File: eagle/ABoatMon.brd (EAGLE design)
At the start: 78.7 x 61 mm, 30 parts, among them J1 5V, J2 GND, J3 GND, J4 5V, X1 MKDSN1,5/2-5,08

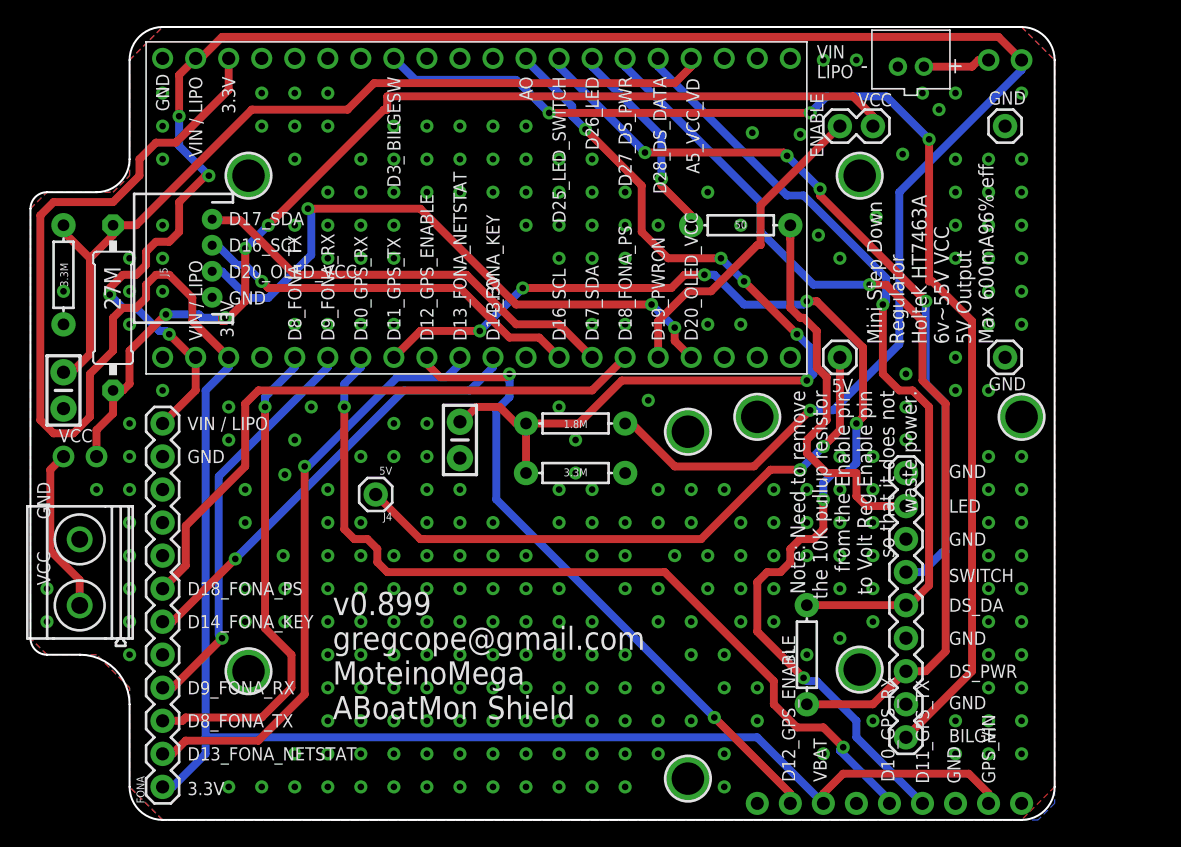
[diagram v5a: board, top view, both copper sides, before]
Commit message: fixed vcc
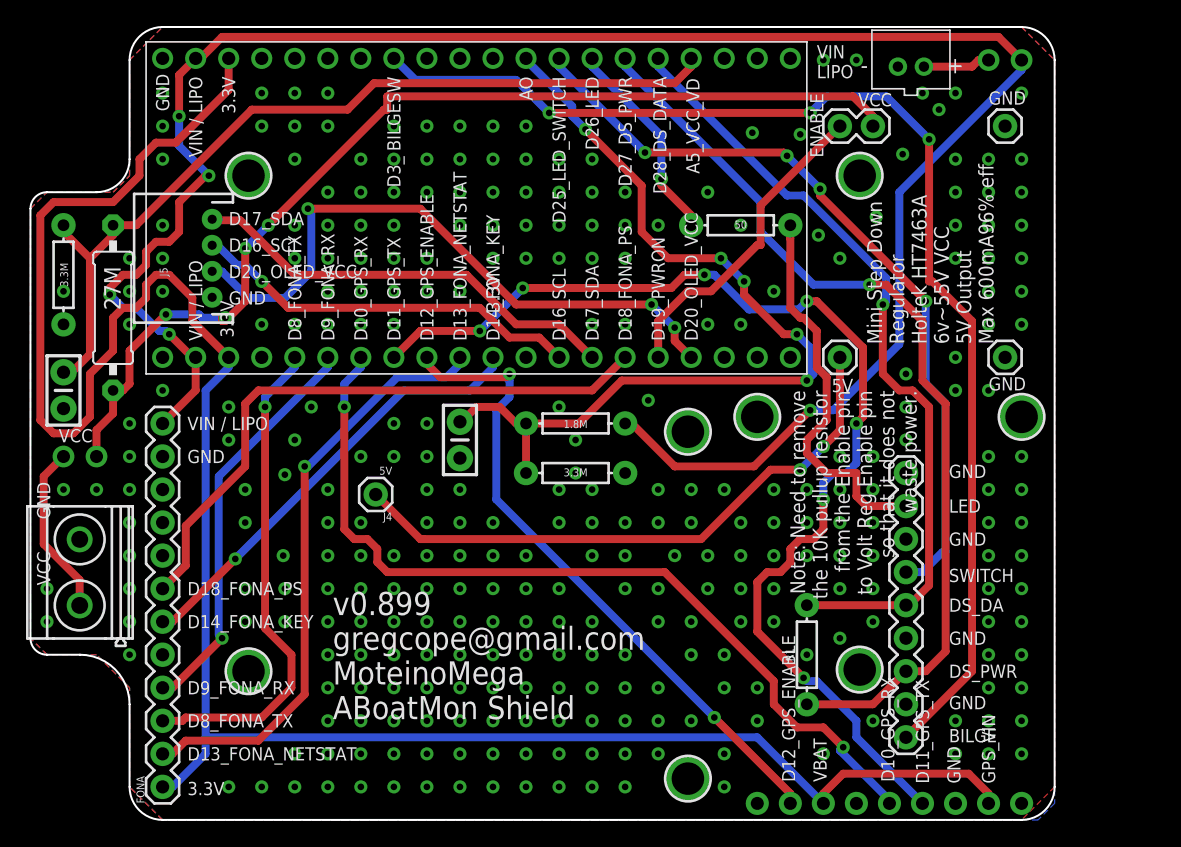
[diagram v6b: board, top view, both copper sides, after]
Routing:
- net D20_OLED_VCC: track 48.4 -> 49.2 mm
- net A0: track 69.4 -> 70.0 mm
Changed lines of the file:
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@@
 <?xml version="1.0" encoding="utf-8"?>
 <!DOCTYPE eagle SYSTEM "eagle.dtd">
-<eagle version="9.1.0">
+<eagle version="9.3.0">
 <drawing>
 <settings>
@@
 <via x="74.93" y="5.08" extent="1-16" drill="0.508"/>
 <via x="8.89" y="12.7" extent="1-16" drill="0.508"/>
-<via x="6.35" y="25.4" extent="1-16" drill="0.508"/>
+<via x="3.81" y="25.4" extent="1-16" drill="0.508"/>
 <via x="2.54" y="17.78" extent="1-16" drill="0.508"/>
 <via x="72.39" y="55.88" extent="1-16" drill="0.508"/>
@@
 <via x="24.13" y="38.1" extent="1-16" drill="0.508"/>
 <via x="26.67" y="38.1" extent="1-16" drill="0.508"/>
-<via x="29.21" y="38.1" extent="1-16" drill="0.508"/>
+<via x="26.67" y="40.64" extent="1-16" drill="0.508"/>
 <via x="24.13" y="43.18" extent="1-16" drill="0.508"/>
 <via x="26.67" y="43.18" extent="1-16" drill="0.508"/>
@@
 <via x="50.8" y="20.32" extent="1-16" drill="0.508"/>
 <via x="58.42" y="25.4" extent="1-16" drill="0.508"/>
+<via x="6.35" y="25.4" extent="1-16" drill="0.508"/>
+<via x="19.05" y="38.1" extent="1-16" drill="0.508"/>
+<via x="31.75" y="43.18" extent="1-16" drill="0.508"/>
+<via x="36.83" y="43.18" extent="1-16" drill="0.508"/>
+<via x="39.37" y="43.18" extent="1-16" drill="0.508"/>
+<via x="36.83" y="45.72" extent="1-16" drill="0.508"/>
+<via x="34.29" y="45.72" extent="1-16" drill="0.508"/>
+<via x="21.59" y="43.18" extent="1-16" drill="0.508"/>
+<via x="24.13" y="40.64" extent="1-16" drill="0.508"/>
+<via x="29.21" y="38.1" extent="1-16" drill="0.508"/>
+<via x="29.21" y="40.64" extent="1-16" drill="0.508"/>
+<via x="31.75" y="40.64" extent="1-16" drill="0.508"/>
+<via x="34.29" y="40.64" extent="1-16" drill="0.508"/>
+<via x="58.42" y="40.64" extent="1-16" drill="0.508"/>
 </signal>
 <signal name="VIN" class="1">
@@
 <wire x1="54.356" y1="43.18" x2="50.292" y2="43.18" width="0.6096" layer="1"/>
 <wire x1="56.134" y1="41.402" x2="54.356" y2="43.18" width="0.6096" layer="16"/>
-<wire x1="60.198" y1="37.338" x2="56.134" y2="41.402" width="0.6096" layer="1"/>
+<wire x1="60.198" y1="37.338" x2="59.182" y2="37.338" width="0.6096" layer="1"/>
+<wire x1="59.182" y1="37.338" x2="56.134" y2="40.386" width="0.6096" layer="1"/>
+<wire x1="56.134" y1="40.386" x2="56.134" y2="41.402" width="0.6096" layer="1"/>
 <wire x1="61.214" y1="36.322" x2="60.198" y2="37.338" width="0.6096" layer="16"/>
 <wire x1="61.214" y1="34.544" x2="61.214" y2="36.322" width="0.6096" layer="16"/>
@@
 <wire x1="46.736" y1="33.782" x2="60.96" y2="33.782" width="0.6096" layer="1"/>
 <wire x1="43.434" y1="30.48" x2="46.736" y2="33.782" width="0.6096" layer="1"/>
-<wire x1="39.624" y1="30.48" x2="43.434" y2="30.48" width="0.6096" layer="1"/>
+<wire x1="39.37" y1="30.48" x2="43.434" y2="30.48" width="0.6096" layer="1"/>
 <wire x1="39.37" y1="58.42" x2="39.37" y2="58.547" width="0.6096" layer="16"/>
-<wire x1="39.624" y1="30.48" x2="39.37" y2="30.48" width="0.6096" layer="1"/>
-<wire x1="39.37" y1="30.226" x2="39.37" y2="26.67" width="0.6096" layer="1"/>
-<wire x1="39.37" y1="30.226" x2="39.37" y2="30.48" width="0.6096" layer="1"/>
+<wire x1="39.37" y1="30.48" x2="39.37" y2="26.67" width="0.6096" layer="1"/>
 <via x="43.942" y="53.086" extent="1-16" drill="0.508"/>
 <via x="54.356" y="43.18" extent="1-16" drill="0.508"/>
@@
 <contactref element="VCC" pad="2"/>
 <contactref element="X1" pad="1"/>
-<wire x1="2.794" y1="26.924" x2="3.81" y2="27.94" width="0.6096" layer="1"/>
-<wire x1="2.794" y1="20.701" x2="2.794" y2="26.924" width="0.6096" layer="1"/>
+<wire x1="2.286" y1="26.416" x2="3.81" y2="27.94" width="0.6096" layer="1"/>
+<wire x1="2.286" y1="21.209" x2="2.286" y2="26.416" width="0.6096" layer="1"/>
 <wire x1="5.055" y1="16.4889" x2="5.055" y2="18.44" width="0.6096" layer="1"/>
-<wire x1="5.055" y1="18.44" x2="2.794" y2="20.701" width="0.6096" layer="1"/>
+<wire x1="5.055" y1="18.44" x2="2.286" y2="21.209" width="0.6096" layer="1"/>
 </signal>
 <signal name="5V" class="1">
@@
 <contactref element="MOTEINO_MEGA" pad="D11"/>
 <contactref element="JP1" pad="4"/>
-<wire x1="61.722" y1="10.668" x2="61.214" y2="10.668" width="0.6096" layer="16"/>
+<wire x1="61.722" y1="10.668" x2="60.96" y2="10.668" width="0.6096" layer="16"/>
 <wire x1="64.77" y1="7.62" x2="61.722" y2="10.668" width="0.6096" layer="16"/>
 <wire x1="64.77" y1="6.35" x2="64.77" y2="7.62" width="0.6096" layer="16"/>
@@
 <wire x1="53.086" y1="41.91" x2="51.562" y2="41.91" width="0.6096" layer="1"/>
 <wire x1="53.848" y1="41.91" x2="53.086" y2="41.91" width="0.6096" layer="16"/>
-<wire x1="56.134" y1="39.624" x2="53.848" y2="41.91" width="0.6096" layer="16"/>
-<wire x1="60.706" y1="39.624" x2="56.134" y2="39.624" width="0.6096" layer="16"/>
-<wire x1="60.96" y1="39.878" x2="60.706" y2="39.624" width="0.6096" layer="16"/>
+<wire x1="56.515" y1="39.243" x2="53.848" y2="41.91" width="0.6096" layer="16"/>
+<wire x1="60.325" y1="39.243" x2="56.515" y2="39.243" width="0.6096" layer="16"/>
+<wire x1="60.96" y1="39.878" x2="60.325" y2="39.243" width="0.6096" layer="16"/>
 <wire x1="61.722" y1="39.878" x2="60.96" y2="39.878" width="0.6096" layer="1"/>
 <wire x1="65.278" y1="36.322" x2="61.722" y2="39.878" width="0.6096" layer="1"/>
@@
 <wire x1="60.706" y1="10.922" x2="57.15" y2="14.478" width="0.6096" layer="1"/>
 <wire x1="60.96" y1="10.668" x2="60.706" y2="10.922" width="0.6096" layer="16"/>
-<wire x1="60.96" y1="10.668" x2="61.214" y2="10.668" width="0.6096" layer="16"/>
 <via x="35.814" y="37.592" extent="1-16" drill="0.508"/>
 <via x="39.116" y="40.894" extent="1-16" drill="0.508"/>
@@
 <wire x1="40.386" y1="37.084" x2="41.91" y2="35.56" width="0.6096" layer="1"/>
 <wire x1="38.1" y1="37.084" x2="40.386" y2="37.084" width="0.6096" layer="1"/>
-<wire x1="34.29" y1="40.894" x2="38.1" y2="37.084" width="0.6096" layer="1"/>
-<wire x1="19.558" y1="40.894" x2="34.29" y2="40.894" width="0.6096" layer="1"/>
-<wire x1="19.05" y1="41.402" x2="19.558" y2="40.894" width="0.6096" layer="1"/>
+<wire x1="35.814" y1="39.37" x2="38.1" y2="37.084" width="0.6096" layer="1"/>
+<wire x1="21.082" y1="39.37" x2="35.814" y2="39.37" width="0.6096" layer="1"/>
+<wire x1="19.05" y1="41.402" x2="21.082" y2="39.37" width="0.6096" layer="1"/>
 <wire x1="17.78" y1="42.672" x2="19.05" y2="41.402" width="0.6096" layer="16"/>
 <wire x1="17.145" y1="42.672" x2="17.78" y2="42.672" width="0.6096" layer="16"/>
@@
 <wire x1="16.002" y1="42.164" x2="15.24" y2="42.164" width="0.6096" layer="16"/>
 <wire x1="18.034" y1="40.132" x2="16.002" y2="42.164" width="0.6096" layer="16"/>
-<wire x1="19.558" y1="40.132" x2="18.034" y2="40.132" width="0.6096" layer="16"/>
-<wire x1="22.86" y1="43.434" x2="19.558" y2="40.132" width="0.6096" layer="16"/>
-<wire x1="22.86" y1="46.99" x2="22.86" y2="43.434" width="0.6096" layer="16"/>
+<wire x1="20.828" y1="40.132" x2="18.034" y2="40.132" width="0.6096" layer="16"/>
+<wire x1="22.86" y1="42.164" x2="20.828" y2="40.132" width="0.6096" layer="16"/>
+<wire x1="22.86" y1="46.99" x2="22.86" y2="42.164" width="0.6096" layer="16"/>
 <wire x1="15.24" y1="42.164" x2="15.24" y2="42.18" width="0.6096" layer="16"/>
 <wire x1="22.86" y1="46.99" x2="22.606" y2="46.99" width="0.6096" layer="16"/>

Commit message: 0.949
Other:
- board size 78.7 x 61 mm -> 86.4 x 61 mm
- board text added: "v0.949 gregcope@gmail.com MoteinoMega ABoatMon Shield"
- board text removed: "v0.899 gregcope@gmail.com MoteinoMega ABoatMon Shield"
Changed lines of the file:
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@@
 <dimension x1="63.5" y1="35.56" x2="76.2" y2="35.56" x3="69.85" y3="34.29" textsize="1.778" layer="25"/>
 <dimension x1="63.5" y1="35.56" x2="63.5" y2="53.34" x3="63.881" y3="44.45" textsize="1.778" layer="25"/>
-<text x="24.511" y="7.747" size="1.778" layer="25">v0.899
+<text x="24.511" y="7.747" size="1.778" layer="25">v0.949
 gregcope@gmail.com
 MoteinoMega
@@
 <wire x1="11.43" y1="60.96" x2="8.89" y2="58.42" width="0.1524" layer="20" curve="90"/>
 <wire x1="11.43" y1="0" x2="8.89" y2="2.54" width="0.1524" layer="20" curve="-90"/>
-<wire x1="80.01" y1="58.42" x2="80.01" y2="2.54" width="0.1524" layer="20"/>
+<wire x1="80.01" y1="58.42" x2="80.01" y2="52.07" width="0.1524" layer="20"/>
+<wire x1="80.01" y1="8.89" x2="80.01" y2="2.54" width="0.1524" layer="20"/>
 <wire x1="2.54" y1="48.26" x2="6.35" y2="48.26" width="0.1524" layer="20"/>
 <wire x1="6.35" y1="48.26" x2="8.89" y2="50.8" width="0.1524" layer="20" curve="90"/>
@@
 <text x="16.51" y="41.656" size="1.016" layer="25" font="vector" ratio="20">D20_OLED_VCC</text>
 <text x="16.51" y="39.624" size="1.016" layer="25" font="vector" ratio="20">GND</text>
+<wire x1="83.82" y1="48.26" x2="85.09" y2="48.26" width="0.1524" layer="20"/>
+<wire x1="85.09" y1="48.26" x2="87.63" y2="45.72" width="0.1524" layer="20" curve="-90"/>
+<wire x1="87.63" y1="45.72" x2="87.63" y2="15.24" width="0.1524" layer="20"/>
+<wire x1="87.63" y1="15.24" x2="85.09" y2="12.7" width="0.1524" layer="20" curve="-90"/>
+<wire x1="85.09" y1="12.7" x2="83.82" y2="12.7" width="0.1524" layer="20"/>
+<wire x1="83.82" y1="12.7" x2="80.01" y2="8.89" width="0.1524" layer="20" curve="90"/>
+<wire x1="80.01" y1="52.07" x2="83.82" y2="48.26" width="0.1524" layer="20" curve="90"/>
 </plain>
 <attributes>
@@
 <contactref element="JP1" pad="3"/>
 <contactref element="MOTEINO_MEGA" pad="GND_2"/>
-<polygon width="0.1524" layer="16" isolate="0.3048">
-<vertex x="8.89" y="58.42"/>
-<vertex x="11.43" y="60.96"/>
-<vertex x="77.47" y="60.96"/>
-<vertex x="80.01" y="58.42"/>
-<vertex x="80.01" y="1.27"/>
-<vertex x="78.74" y="0"/>
-<vertex x="11.43" y="0"/>
-<vertex x="8.89" y="2.54"/>
-<vertex x="8.89" y="10.16"/>
-<vertex x="6.35" y="12.7"/>
-<vertex x="2.54" y="12.7"/>
-<vertex x="1.27" y="13.97"/>
-<vertex x="1.27" y="46.99"/>
-<vertex x="2.54" y="48.26"/>
-<vertex x="7.62" y="48.26"/>
-<vertex x="8.89" y="49.53"/>
-</polygon>
 <contactref element="JST" pad="7"/>
 <contactref element="JST" pad="2"/>
@@
 <via x="41.91" y="50.8" extent="1-16" drill="0.508"/>
 <via x="44.45" y="50.8" extent="1-16" drill="0.508"/>
-<polygon width="0.1524" layer="1" isolate="0.3048">
-<vertex x="11.43" y="60.96"/>
-<vertex x="77.47" y="60.96"/>
-<vertex x="80.01" y="58.42"/>
-<vertex x="80.01" y="2.54"/>
-<vertex x="77.47" y="0"/>
-<vertex x="11.43" y="0"/>
-<vertex x="8.89" y="2.54"/>
-<vertex x="8.89" y="10.16"/>
-<vertex x="6.35" y="12.7"/>
-<vertex x="2.54" y="12.7"/>
-<vertex x="1.27" y="13.97"/>
-<vertex x="1.27" y="46.99"/>
-<vertex x="2.54" y="48.26"/>
-<vertex x="7.62" y="48.26"/>
-<vertex x="8.89" y="49.53"/>
-<vertex x="8.89" y="58.42"/>
-</polygon>
 <via x="31.75" y="22.86" extent="1-16" drill="0.508"/>
 <via x="34.29" y="22.86" extent="1-16" drill="0.508"/>
@@
 <via x="36.83" y="45.72" extent="1-16" drill="0.508"/>
 <via x="34.29" y="45.72" extent="1-16" drill="0.508"/>
-<via x="21.59" y="43.18" extent="1-16" drill="0.508"/>
 <via x="24.13" y="40.64" extent="1-16" drill="0.508"/>
 <via x="29.21" y="38.1" extent="1-16" drill="0.508"/>
@@
 <via x="34.29" y="40.64" extent="1-16" drill="0.508"/>
 <via x="58.42" y="40.64" extent="1-16" drill="0.508"/>
+<polygon width="0.1524" layer="1">
+<vertex x="11.43" y="60.96"/>
+<vertex x="77.47" y="60.96"/>
+<vertex x="80.01" y="58.42"/>
+<vertex x="80.01" y="50.8"/>
+<vertex x="82.55" y="48.26"/>
+<vertex x="86.36" y="48.26"/>
+<vertex x="87.63" y="46.99"/>
+<vertex x="87.63" y="15.24"/>
+<vertex x="86.36" y="12.7"/>
+<vertex x="82.55" y="12.7"/>
+<vertex x="80.01" y="10.16"/>
+<vertex x="80.01" y="2.54"/>
+<vertex x="78.74" y="0"/>
+<vertex x="11.43" y="0"/>
+<vertex x="8.89" y="2.54"/>
+<vertex x="8.89" y="10.16"/>
+<vertex x="6.35" y="12.7"/>
+<vertex x="2.54" y="12.7"/>
+<vertex x="1.27" y="13.97"/>
+<vertex x="1.27" y="46.99"/>
+<vertex x="2.54" y="48.26"/>
+<vertex x="6.35" y="48.26"/>
+<vertex x="8.89" y="49.53"/>
+<vertex x="8.89" y="58.42"/>
+</polygon>
+<polygon width="0.1524" layer="1">
+<vertex x="11.43" y="60.96"/>
+<vertex x="77.47" y="60.96"/>
+<vertex x="80.01" y="58.42"/>
+<vertex x="80.01" y="50.8"/>
+<vertex x="82.55" y="48.26"/>
+<vertex x="86.36" y="48.26"/>
+<vertex x="87.63" y="46.99"/>
+<vertex x="87.63" y="15.24"/>
+<vertex x="86.36" y="12.7"/>
+<vertex x="82.55" y="12.7"/>
+<vertex x="80.01" y="10.16"/>
+<vertex x="80.01" y="2.54"/>
+<vertex x="78.74" y="0"/>
+<vertex x="11.43" y="0"/>
+<vertex x="8.89" y="2.54"/>
+<vertex x="8.89" y="10.16"/>
+<vertex x="6.35" y="12.7"/>
+<vertex x="2.54" y="12.7"/>
+<vertex x="1.27" y="13.97"/>
+<vertex x="1.27" y="46.99"/>
+<vertex x="2.54" y="48.26"/>
+<vertex x="6.35" y="48.26"/>
+<vertex x="8.89" y="49.53"/>
+<vertex x="8.89" y="58.42"/>
+</polygon>
+<polygon width="0.1524" layer="16">
+<vertex x="8.89" y="58.42"/>
+<vertex x="11.43" y="60.96"/>
+<vertex x="77.47" y="60.96"/>
+<vertex x="80.01" y="58.42"/>
+<vertex x="80.01" y="50.8"/>
+<vertex x="82.55" y="48.26"/>
+<vertex x="86.36" y="48.26"/>
+<vertex x="87.63" y="46.99"/>
+<vertex x="87.63" y="15.24"/>
+<vertex x="86.36" y="12.7"/>
+<vertex x="82.55" y="12.7"/>
+<vertex x="80.01" y="10.16"/>
+<vertex x="80.01" y="2.54"/>
+<vertex x="78.74" y="0"/>
+<vertex x="11.43" y="0"/>
+<vertex x="8.89" y="2.54"/>
+<vertex x="8.89" y="10.16"/>
+<vertex x="6.35" y="12.7"/>
+<vertex x="2.54" y="12.7"/>
+<vertex x="1.27" y="13.97"/>
+<vertex x="1.27" y="46.99"/>
+<vertex x="2.54" y="48.26"/>
+<vertex x="6.35" y="48.26"/>
+<vertex x="8.89" y="49.53"/>
+</polygon>
+<via x="80.01" y="48.26" extent="1-16" drill="0.508"/>
+<via x="80.01" y="12.7" extent="1-16" drill="0.508"/>
+<via x="80.01" y="17.78" extent="1-16" drill="0.508"/>
+<via x="80.01" y="15.24" extent="1-16" drill="0.508"/>
+<via x="80.01" y="20.32" extent="1-16" drill="0.508"/>
+<via x="82.55" y="17.78" extent="1-16" drill="0.508"/>
+<via x="82.55" y="15.24" extent="1-16" drill="0.508"/>
+<via x="82.55" y="20.32" extent="1-16" drill="0.508"/>
+<via x="82.55" y="25.4" extent="1-16" drill="0.508"/>
+<via x="82.55" y="30.48" extent="1-16" drill="0.508"/>
+<via x="82.55" y="27.94" extent="1-16" drill="0.508"/>
+<via x="82.55" y="33.02" extent="1-16" drill="0.508"/>
+<via x="82.55" y="22.86" extent="1-16" drill="0.508"/>
+<via x="85.09" y="25.4" extent="1-16" drill="0.508"/>
+<via x="85.09" y="30.48" extent="1-16" drill="0.508"/>
+<via x="85.09" y="27.94" extent="1-16" drill="0.508"/>
+<via x="85.09" y="33.02" extent="1-16" drill="0.508"/>
+<via x="85.09" y="22.86" extent="1-16" drill="0.508"/>
+<via x="80.01" y="25.4" extent="1-16" drill="0.508"/>
+<via x="80.01" y="27.94" extent="1-16" drill="0.508"/>
+<via x="80.01" y="33.02" extent="1-16" drill="0.508"/>
+<via x="80.01" y="22.86" extent="1-16" drill="0.508"/>
+<via x="85.09" y="17.78" extent="1-16" drill="0.508"/>
+<via x="85.09" y="15.24" extent="1-16" drill="0.508"/>
+<via x="85.09" y="20.32" extent="1-16" drill="0.508"/>
+<via x="80.01" y="38.1" extent="1-16" drill="0.508"/>
+<via x="80.01" y="43.18" extent="1-16" drill="0.508"/>
+<via x="80.01" y="40.64" extent="1-16" drill="0.508"/>
+<via x="80.01" y="45.72" extent="1-16" drill="0.508"/>
+<via x="80.01" y="35.56" extent="1-16" drill="0.508"/>
+<via x="82.55" y="38.1" extent="1-16" drill="0.508"/>
+<via x="82.55" y="43.18" extent="1-16" drill="0.508"/>
+<via x="82.55" y="40.64" extent="1-16" drill="0.508"/>
+<via x="82.55" y="45.72" extent="1-16" drill="0.508"/>
+<via x="82.55" y="35.56" extent="1-16" drill="0.508"/>
+<via x="85.09" y="38.1" extent="1-16" drill="0.508"/>
+<via x="85.09" y="43.18" extent="1-16" drill="0.508"/>
+<via x="85.09" y="40.64" extent="1-16" drill="0.508"/>
+<via x="85.09" y="45.72" extent="1-16" drill="0.508"/>
+<via x="85.09" y="35.56" extent="1-16" drill="0.508"/>
 </signal>
 <signal name="VIN" class="1">
